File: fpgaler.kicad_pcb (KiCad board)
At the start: 2 copper layers, 0 parts

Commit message: start to assign footprint
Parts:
- added C1: 100nF, Capacitor_SMD:C_0603_1608Metric, F.Cu at (130.2, 113.1)
- added C10: 4.7uF, Capacitor_SMD:C_0805_2012Metric, F.Cu at (169.7, 49.9)
- added C11: 4.7uF, Capacitor_SMD:C_0805_2012Metric, F.Cu at (169.7, 52.9)
- added C12: 10uF, Capacitor_SMD:C_1206_3216Metric, F.Cu at (164.7, 50.1)
- added C13: 10uF, Capacitor_SMD:C_1206_3216Metric, F.Cu at (164.7, 53.5)
- added C14: 4.7uF, Capacitor_SMD:C_0805_2012Metric, F.Cu at (169.7, 56.0)
- added C15: 10pF, Capacitor_SMD:C_0603_1608Metric, F.Cu at (151.8, 52.2)
- added C16: 10pF, Capacitor_SMD:C_0603_1608Metric, F.Cu at (151.8, 54.7)
- added C17: 4.7uF, Capacitor_SMD:C_0805_2012Metric, F.Cu at (169.7, 59.0)
- added C18: 10uF, Capacitor_SMD:C_1206_3216Metric, F.Cu at (164.7, 56.8)
- added C19: 10uF, Capacitor_SMD:C_1206_3216Metric, F.Cu at (164.7, 60.1)
- added C2: 4.7uF, Capacitor_SMD:C_0805_2012Metric, F.Cu at (113.3, 131.0)
- added C20: 10uF, Capacitor_SMD:C_1206_3216Metric, F.Cu at (164.7, 63.5)
- added C21: 10uF, Capacitor_SMD:C_1206_3216Metric, F.Cu at (164.7, 66.8)
- added C22: 100nF, Capacitor_SMD:C_0603_1608Metric, F.Cu at (148.3, 90.7)
- added C23: 18pF, Capacitor_SMD:C_0603_1608Metric, F.Cu at (148.3, 93.2)
- added C24: 18pF, Capacitor_SMD:C_0603_1608Metric, F.Cu at (148.3, 95.8)
- added C25: 10uF, Capacitor_SMD:C_1206_3216Metric, F.Cu at (165.1, 105.6)
- added C26: 100nF, Capacitor_SMD:C_0603_1608Metric, F.Cu at (148.3, 98.3)
- added C27: 100nF, Capacitor_SMD:C_0603_1608Metric, F.Cu at (148.3, 100.8)
- added C28: 100nF, Capacitor_SMD:C_0603_1608Metric, F.Cu at (148.3, 103.3)
- added C29: 100nF, Capacitor_SMD:C_0603_1608Metric, F.Cu at (148.3, 105.8)
- added C3: 100nF, Capacitor_SMD:C_0603_1608Metric, F.Cu at (130.2, 115.6)
- added C30: 100nF, Capacitor_SMD:C_0603_1608Metric, F.Cu at (148.3, 108.3)
- added C31: 100nF, Capacitor_SMD:C_0603_1608Metric, F.Cu at (148.3, 110.8)
- added C32: 100nF, Capacitor_SMD:C_0603_1608Metric, F.Cu at (152.3, 90.7)
- added C33: 10uF, Capacitor_SMD:C_1206_3216Metric, F.Cu at (165.1, 109.0)
- added C34: 100nF, Capacitor_SMD:C_0603_1608Metric, F.Cu at (152.3, 93.2)
- added C35: 100nF, Capacitor_SMD:C_0603_1608Metric, F.Cu at (152.3, 95.8)
- added C36: 4.7uF, Capacitor_SMD:C_0805_2012Metric, F.Cu at (170.2, 105.4)
- added C37: 4.7uF, Capacitor_SMD:C_0805_2012Metric, F.Cu at (170.2, 108.4)
- added C38: 100nF, Capacitor_SMD:C_0603_1608Metric, F.Cu at (129.8, 49.7)
- added C39: 100nF, Capacitor_SMD:C_0603_1608Metric, F.Cu at (129.8, 52.2)
- added C4: 100nF, Capacitor_SMD:C_0603_1608Metric, F.Cu at (130.2, 118.1)
- added C40: 10nF, Capacitor_SMD:C_0603_1608Metric, F.Cu at (148.3, 117.8)
- added C41: 10nF, Capacitor_SMD:C_0603_1608Metric, F.Cu at (148.3, 120.3)
- added C42: 10nF, Capacitor_SMD:C_0603_1608Metric, F.Cu at (148.3, 122.8)
- added C43: 100nF, Capacitor_SMD:C_0603_1608Metric, F.Cu at (148.3, 125.3)
- added C44: 100nF, Capacitor_SMD:C_0603_1608Metric, F.Cu at (148.3, 127.8)
- added C45: 100nF, Capacitor_SMD:C_0603_1608Metric, F.Cu at (148.3, 130.3)
- added C46: 10nF, Capacitor_SMD:C_0603_1608Metric, F.Cu at (148.3, 132.8)
- added C47: 10nF, Capacitor_SMD:C_0603_1608Metric, F.Cu at (152.3, 117.8)
- added C48: 10nF, Capacitor_SMD:C_0603_1608Metric, F.Cu at (152.3, 120.3)
- added C49: 100nF, Capacitor_SMD:C_0603_1608Metric, F.Cu at (152.3, 122.8)
- added C5: 100nF, Capacitor_SMD:C_0603_1608Metric, F.Cu at (130.2, 120.6)
- added C50: 100nF, Capacitor_SMD:C_0603_1608Metric, F.Cu at (152.3, 125.3)
- added C51: 100nF, Capacitor_SMD:C_0603_1608Metric, F.Cu at (152.3, 127.8)
- added C52: 10nF, Capacitor_SMD:C_0603_1608Metric, F.Cu at (152.3, 130.3)
- added C53: 10nF, Capacitor_SMD:C_0603_1608Metric, F.Cu at (152.3, 132.8)
- added C54: 100nF, Capacitor_SMD:C_0603_1608Metric, F.Cu at (156.3, 117.8)
- added C55: 100nF, Capacitor_SMD:C_0603_1608Metric, F.Cu at (156.3, 120.3)
- added C6: 100nF, Capacitor_SMD:C_0603_1608Metric, F.Cu at (130.2, 123.1)
- added C7: 100nF, Capacitor_SMD:C_0603_1608Metric, F.Cu at (130.2, 125.7)
- added C8: 100nF, Capacitor_SMD:C_0603_1608Metric, F.Cu at (130.2, 128.2)
- added C9: 100nF, Capacitor_SMD:C_0603_1608Metric, F.Cu at (151.8, 49.7)
- added D1: L0, Diode_SMD:D_0603_1608Metric, F.Cu at (134.8, 90.8)
- added D10: LED, Diode_SMD:D_0603_1608Metric, F.Cu at (164.3, 124.9)
- added D11: LED, Diode_SMD:D_0603_1608Metric, F.Cu at (164.3, 127.5)
- added D2: L1, Diode_SMD:D_0603_1608Metric, F.Cu at (134.8, 93.4)
- added D3: L2, Diode_SMD:D_0603_1608Metric, F.Cu at (134.8, 96.0)
- added D4: L3, Diode_SMD:D_0603_1608Metric, F.Cu at (134.8, 98.5)
- added D5: L4, Diode_SMD:D_0603_1608Metric, F.Cu at (134.8, 101.1)
- added D6: L5, Diode_SMD:D_0603_1608Metric, F.Cu at (134.8, 103.7)
- added D7: L6, Diode_SMD:D_0603_1608Metric, F.Cu at (134.8, 106.3)
- added D8: L7, Diode_SMD:D_0603_1608Metric, F.Cu at (134.8, 108.9)
- added FB2: BLM18HE152SN1D, Inductor_SMD:L_0603_1608Metric, F.Cu at (152.3, 98.3)
- added FB3: BLM18HE152SN1D, Inductor_SMD:L_0603_1608Metric, F.Cu at (152.3, 100.8)
- added J1: USB_C_Receptacle_USB2.0, Connector_USB:USB_C_Receptacle_HRO_TYPE-C-31-M-12, F.Cu at (105.2, 128.2)
- added J3: Conn_01x08_MountingPin, Connector_PinHeader_2.54mm:PinHeader_1x08_P2.54mm_Vertical, F.Cu at (130.5, 91.8)
- added J4: FTDI_RST, Connector_PinHeader_2.54mm:PinHeader_1x02_P2.54mm_Vertical, F.Cu at (113.3, 124.7)
- added L1: 2.2uH, Inductor_SMD:L_0805_2012Metric, F.Cu at (157.7, 64.9)
- added L2: 2.2uH, Inductor_SMD:L_0805_2012Metric, F.Cu at (157.7, 67.6)
- added Q1: 2N2222/SOT23, Package_TO_SOT_SMD:SOT-23-3, F.Cu at (164.9, 131.0)
- added R1: 10k, Resistor_SMD:R_0603_1608Metric, F.Cu at (130.2, 130.7)
- added R10: 22R, Resistor_SMD:R_0603_1608Metric, F.Cu at (138.2, 113.1)
- added R11: 10k, Resistor_SMD:R_0603_1608Metric, F.Cu at (138.2, 115.6)
- added R12: 1.2k, Resistor_SMD:R_0603_1608Metric, F.Cu at (138.2, 118.1)
- added R13: 1.2k, Resistor_SMD:R_0603_1608Metric, F.Cu at (138.2, 120.6)
- added R14: 1.2k, Resistor_SMD:R_0603_1608Metric, F.Cu at (138.2, 123.1)
- added R15: 10k, Resistor_SMD:R_0603_1608Metric, F.Cu at (138.2, 125.7)
- added R16: 1.2k, Resistor_SMD:R_0603_1608Metric, F.Cu at (138.2, 128.2)
- added R17: 10k, Resistor_SMD:R_0603_1608Metric, F.Cu at (138.2, 130.7)
- added R18: 1.2k, Resistor_SMD:R_0603_1608Metric, F.Cu at (142.2, 113.1)
- added R19: 10k, Resistor_SMD:R_0603_1608Metric, F.Cu at (142.2, 115.6)
- added R2: 10k, Resistor_SMD:R_0603_1608Metric, F.Cu at (134.2, 113.1)
- added R20: 1.2k, Resistor_SMD:R_0603_1608Metric, F.Cu at (142.2, 118.1)
- added R21: 1.2k, Resistor_SMD:R_0603_1608Metric, F.Cu at (142.2, 120.6)
- added R22: 10k, Resistor_SMD:R_0603_1608Metric, F.Cu at (142.2, 123.1)
- added R23: 1.2k, Resistor_SMD:R_0603_1608Metric, F.Cu at (142.2, 125.7)
- added R24: 10k, Resistor_SMD:R_0603_1608Metric, F.Cu at (142.2, 128.2)
- added R25: 10k, Resistor_SMD:R_0603_1608Metric, F.Cu at (151.8, 57.2)
- added R26: 4.7k, Resistor_SMD:R_0603_1608Metric, F.Cu at (151.8, 59.7)
- added R27: 3.57k, Resistor_SMD:R_0603_1608Metric, F.Cu at (151.8, 62.2)
- added R28: 56.2k, Resistor_SMD:R_0603_1608Metric, F.Cu at (155.8, 49.7)
- added R29: 3.09k, Resistor_SMD:R_0603_1608Metric, F.Cu at (155.8, 52.2)
- added R3: 10k, Resistor_SMD:R_0603_1608Metric, F.Cu at (134.2, 115.6)
- added R30: 4.32k, Resistor_SMD:R_0603_1608Metric, F.Cu at (155.8, 54.7)
- added R31: 10k, Resistor_SMD:R_0603_1608Metric, F.Cu at (155.8, 57.2)
- added R32: 10k, Resistor_SMD:R_0603_1608Metric, F.Cu at (155.8, 59.7)
- added R33: DNP, Resistor_SMD:R_0603_1608Metric, F.Cu at (155.8, 62.2)
- added R34: 100k, Resistor_SMD:R_0603_1608Metric, F.Cu at (159.8, 49.7)
- added R35: 120k, Resistor_SMD:R_0603_1608Metric, F.Cu at (159.8, 52.2)
- added R36: 360k, Resistor_SMD:R_0603_1608Metric, F.Cu at (159.8, 54.7)
- added R37: 82k, Resistor_SMD:R_0603_1608Metric, F.Cu at (159.8, 57.2)
- added R38: 10k, Resistor_SMD:R_0603_1608Metric, F.Cu at (152.3, 103.3)
- added R39: 10k, Resistor_SMD:R_0603_1608Metric, F.Cu at (152.3, 105.8)
- added R4: 10k, Resistor_SMD:R_0603_1608Metric, F.Cu at (134.2, 118.1)
- added R40: 10k, Resistor_SMD:R_0603_1608Metric, F.Cu at (152.3, 108.3)
- added R41: 12k, Resistor_SMD:R_0603_1608Metric, F.Cu at (152.3, 110.8)
- added R42: 2.2k, Resistor_SMD:R_0603_1608Metric, F.Cu at (156.3, 90.7)
- added R43: 0R, Resistor_SMD:R_0603_1608Metric, F.Cu at (156.3, 93.2)
- added R44: 12k, Resistor_SMD:R_0603_1608Metric, F.Cu at (156.3, 95.8)
- added R45: 2.2k, Resistor_SMD:R_0603_1608Metric, F.Cu at (156.3, 98.3)
- added R46: 22R, Resistor_SMD:R_0603_1608Metric, F.Cu at (156.3, 100.8)
- added R47: 22R, Resistor_SMD:R_0603_1608Metric, F.Cu at (156.3, 103.3)
- added R48: 22R, Resistor_SMD:R_0603_1608Metric, F.Cu at (156.3, 105.8)
- added R49: 22R, Resistor_SMD:R_0603_1608Metric, F.Cu at (156.3, 108.3)
- added R5: 5.1k, Resistor_SMD:R_0603_1608Metric, F.Cu at (134.2, 120.6)
- added R50: 22R, Resistor_SMD:R_0603_1608Metric, F.Cu at (156.3, 110.8)
- added R51: 22R, Resistor_SMD:R_0603_1608Metric, F.Cu at (160.3, 90.7)
- added R52: 2.2k, Resistor_SMD:R_0603_1608Metric, F.Cu at (160.3, 93.2)
- added R53: 22R, Resistor_SMD:R_0603_1608Metric, F.Cu at (160.3, 95.8)
- added R54: 22R, Resistor_SMD:R_0603_1608Metric, F.Cu at (160.3, 98.3)
- added R55: 22R, Resistor_SMD:R_0603_1608Metric, F.Cu at (160.3, 100.8)
- added R56: 2.2k, Resistor_SMD:R_0603_1608Metric, F.Cu at (160.3, 103.3)
- added R57: 4.7k, Resistor_SMD:R_0603_1608Metric, F.Cu at (160.3, 105.8)
- added R58: 4.7k, Resistor_SMD:R_0603_1608Metric, F.Cu at (160.3, 108.3)
- added R59: 4.7k, Resistor_SMD:R_0603_1608Metric, F.Cu at (160.3, 110.8)
- added R6: 5.1k, Resistor_SMD:R_0603_1608Metric, F.Cu at (134.2, 123.1)
- added R60: 4.7k, Resistor_SMD:R_0603_1608Metric, F.Cu at (129.8, 54.7)
- added R61: 22R, Resistor_SMD:R_0603_1608Metric, F.Cu at (129.8, 57.2)
- added R62: 22R, Resistor_SMD:R_0603_1608Metric, F.Cu at (129.8, 59.7)
- added R63: 22R, Resistor_SMD:R_0603_1608Metric, F.Cu at (129.8, 62.2)
- added R64: 22R, Resistor_SMD:R_0603_1608Metric, F.Cu at (133.8, 49.7)
- added R65: 4.7k, Resistor_SMD:R_0603_1608Metric, F.Cu at (133.8, 52.2)
- added R66: 4.7k, Resistor_SMD:R_0603_1608Metric, F.Cu at (133.8, 54.7)
- added R67: 22R, Resistor_SMD:R_0603_1608Metric, F.Cu at (133.8, 57.2)
- added R68: 22R, Resistor_SMD:R_0603_1608Metric, F.Cu at (133.8, 59.7)
- added R69: 22R, Resistor_SMD:R_0603_1608Metric, F.Cu at (133.8, 62.2)
- added R7: 10k, Resistor_SMD:R_0603_1608Metric, F.Cu at (134.2, 125.7)
- added R70: 22R, Resistor_SMD:R_0603_1608Metric, F.Cu at (137.8, 49.7)
- added R71: 22R, Resistor_SMD:R_0603_1608Metric, F.Cu at (137.8, 52.2)
- added R72: 22R, Resistor_SMD:R_0603_1608Metric, F.Cu at (137.8, 54.7)
- added R73: 22R, Resistor_SMD:R_0603_1608Metric, F.Cu at (137.8, 57.2)
- added R74: 22R, Resistor_SMD:R_0603_1608Metric, F.Cu at (137.8, 59.7)
- added R75: 22R, Resistor_SMD:R_0603_1608Metric, F.Cu at (137.8, 62.2)
- added R76: 22R, Resistor_SMD:R_0603_1608Metric, F.Cu at (141.8, 49.7)
- added R77: 22R, Resistor_SMD:R_0603_1608Metric, F.Cu at (141.8, 52.2)
- added R78: 22R, Resistor_SMD:R_0603_1608Metric, F.Cu at (141.8, 54.7)
- added R79: 22R, Resistor_SMD:R_0603_1608Metric, F.Cu at (141.8, 57.2)
- added R8: 10k, Resistor_SMD:R_0603_1608Metric, F.Cu at (134.2, 128.2)
- added R80: 22R, Resistor_SMD:R_0603_1608Metric, F.Cu at (141.8, 59.7)
- added R81: 22R, Resistor_SMD:R_0603_1608Metric, F.Cu at (141.8, 62.2)
- added R82: 22R, Resistor_SMD:R_0603_1608Metric, F.Cu at (145.8, 49.7)
- added R83: 22R, Resistor_SMD:R_0603_1608Metric, F.Cu at (145.8, 52.2)
- added R84: 22R, Resistor_SMD:R_0603_1608Metric, F.Cu at (145.8, 54.7)
- added R85: 4.7k, Resistor_SMD:R_0603_1608Metric, F.Cu at (145.8, 57.2)
- added R86: 4.7k, Resistor_SMD:R_0603_1608Metric, F.Cu at (145.8, 59.7)
- added R87: 4.7k, Resistor_SMD:R_0603_1608Metric, F.Cu at (145.8, 62.2)
- added R88: 1.5k, Resistor_SMD:R_0603_1608Metric, F.Cu at (156.3, 122.8)
- added R89: 2.2k, Resistor_SMD:R_0603_1608Metric, F.Cu at (156.3, 125.3)
- added R9: 22R, Resistor_SMD:R_0603_1608Metric, F.Cu at (134.2, 130.7)
- added R90: 4.7k, Resistor_SMD:R_0603_1608Metric, F.Cu at (156.3, 127.8)
- added R91: 4.7k, Resistor_SMD:R_0603_1608Metric, F.Cu at (156.3, 130.3)
- added R92: 4.7k, Resistor_SMD:R_0603_1608Metric, F.Cu at (156.3, 132.8)
- added R93: 2.2k, Resistor_SMD:R_0603_1608Metric, F.Cu at (160.3, 117.8)
- added R94: 2.2k, Resistor_SMD:R_0603_1608Metric, F.Cu at (160.3, 120.3)
- added R95: 10k, Resistor_SMD:R_0603_1608Metric, F.Cu at (160.3, 122.8)
- added R96: 10k, Resistor_SMD:R_0603_1608Metric, F.Cu at (160.3, 125.3)
- added SW1: RotaryEncoder_Switch, Rotary_Encoder:RotaryEncoder_Alps_EC11E-Switch_Vertical_H20mm_CircularMountingHoles, F.Cu at (101.4, 95.2)
- added SW2: RotaryEncoder_Switch, Rotary_Encoder:RotaryEncoder_Alps_EC11E-Switch_Vertical_H20mm_CircularMountingHoles, F.Cu at (101.4, 111.7)
- added SW3: K1, Button_Switch_THT:SW_PUSH_1P1T_6x3.5mm_H4.3_APEM_MJTP1243, F.Cu at (119.8, 92.0)
- added SW4: K2, Button_Switch_THT:SW_PUSH_1P1T_6x3.5mm_H4.3_APEM_MJTP1243, F.Cu at (119.8, 97.0)
- added SW5: PROGRAMN, Button_Switch_THT:SW_PUSH_1P1T_6x3.5mm_H4.3_APEM_MJTP1243, F.Cu at (119.8, 102.1)
- added SW6: K3, Button_Switch_THT:SW_PUSH_1P1T_6x3.5mm_H4.3_APEM_MJTP1243, F.Cu at (119.8, 107.2)
- added SW7: FPGA GSRN, Button_Switch_THT:SW_PUSH_1P1T_6x3.5mm_H4.3_APEM_MJTP1243, F.Cu at (119.8, 112.2)
- added SW8: K4, Button_Switch_THT:SW_PUSH_1P1T_6x3.5mm_H4.3_APEM_MJTP1243, F.Cu at (119.8, 117.2)
- added TP1: TestPoint, TestPoint:TestPoint_Pad_D1.0mm, F.Cu at (174.7, 111.5)
- added TP10: TestPoint, TestPoint:TestPoint_THTPad_D1.5mm_Drill0.7mm, F.Cu at (101.1, 78.6)
- added TP11: TestPoint, TestPoint:TestPoint_THTPad_D1.5mm_Drill0.7mm, F.Cu at (101.1, 82.2)
- added TP12: TestPoint, TestPoint:TestPoint_THTPad_D1.5mm_Drill0.7mm, F.Cu at (101.1, 85.7)
- added TP13: TestPoint, TestPoint:TestPoint_THTPad_D1.5mm_Drill0.7mm, F.Cu at (104.7, 50.2)
- added TP14: TestPoint, TestPoint:TestPoint_THTPad_D1.5mm_Drill0.7mm, F.Cu at (104.7, 53.8)
- added TP15: TestPoint, TestPoint:TestPoint_THTPad_D1.5mm_Drill0.7mm, F.Cu at (104.7, 57.3)
- added TP16: TestPoint, TestPoint:TestPoint_THTPad_D1.5mm_Drill0.7mm, F.Cu at (104.7, 60.9)
- added TP17: TestPoint, TestPoint:TestPoint_THTPad_D1.5mm_Drill0.7mm, F.Cu at (104.7, 64.4)
- added TP18: TestPoint, TestPoint:TestPoint_THTPad_D1.5mm_Drill0.7mm, F.Cu at (104.7, 68.0)
- added TP19: TestPoint, TestPoint:TestPoint_THTPad_D1.5mm_Drill0.7mm, F.Cu at (104.7, 71.5)
- added TP2: TestPoint, TestPoint:TestPoint_THTPad_D1.5mm_Drill0.7mm, F.Cu at (101.1, 50.2)
- added TP20: TestPoint, TestPoint:TestPoint_THTPad_D1.5mm_Drill0.7mm, F.Cu at (104.7, 75.0)
- added TP21: TestPoint, TestPoint:TestPoint_THTPad_D1.5mm_Drill0.7mm, F.Cu at (104.7, 78.6)
- added TP22: TestPoint, TestPoint:TestPoint_THTPad_D1.5mm_Drill0.7mm, F.Cu at (104.7, 82.2)
- added TP23: TestPoint, TestPoint:TestPoint_THTPad_D1.5mm_Drill0.7mm, F.Cu at (104.7, 85.7)
- added TP24: TestPoint, TestPoint:TestPoint_THTPad_D1.5mm_Drill0.7mm, F.Cu at (108.2, 50.2)
- added TP25: TestPoint, TestPoint:TestPoint_THTPad_D1.5mm_Drill0.7mm, F.Cu at (108.2, 53.8)
- added TP26: TestPoint, TestPoint:TestPoint_THTPad_D1.5mm_Drill0.7mm, F.Cu at (108.2, 57.3)
- added TP27: TestPoint, TestPoint:TestPoint_THTPad_D1.5mm_Drill0.7mm, F.Cu at (108.2, 60.9)
- added TP28: TestPoint, TestPoint:TestPoint_THTPad_D1.5mm_Drill0.7mm, F.Cu at (108.2, 64.4)
- added TP29: TestPoint, TestPoint:TestPoint_THTPad_D1.5mm_Drill0.7mm, F.Cu at (108.2, 68.0)
- added TP3: TestPoint, TestPoint:TestPoint_THTPad_D1.5mm_Drill0.7mm, F.Cu at (101.1, 53.8)
- added TP30: TestPoint, TestPoint:TestPoint_THTPad_D1.5mm_Drill0.7mm, F.Cu at (108.2, 71.5)
- added TP31: TestPoint, TestPoint:TestPoint_THTPad_D1.5mm_Drill0.7mm, F.Cu at (108.2, 75.0)
- added TP32: TestPoint, TestPoint:TestPoint_THTPad_D1.5mm_Drill0.7mm, F.Cu at (108.2, 78.6)
- added TP33: TestPoint, TestPoint:TestPoint_THTPad_D1.5mm_Drill0.7mm, F.Cu at (108.2, 82.2)
- added TP34: TestPoint, TestPoint:TestPoint_THTPad_D1.5mm_Drill0.7mm, F.Cu at (108.2, 85.7)
- added TP35: TestPoint, TestPoint:TestPoint_THTPad_D1.5mm_Drill0.7mm, F.Cu at (111.8, 50.2)
- added TP36: TestPoint, TestPoint:TestPoint_THTPad_D1.5mm_Drill0.7mm, F.Cu at (111.8, 53.8)
- added TP37: TestPoint, TestPoint:TestPoint_THTPad_D1.5mm_Drill0.7mm, F.Cu at (111.8, 57.3)
- added TP38: TestPoint, TestPoint:TestPoint_THTPad_D1.5mm_Drill0.7mm, F.Cu at (111.8, 60.9)
- added TP39: TestPoint, TestPoint:TestPoint_THTPad_D1.5mm_Drill0.7mm, F.Cu at (111.8, 64.4)
- added TP4: TestPoint, TestPoint:TestPoint_THTPad_D1.5mm_Drill0.7mm, F.Cu at (101.1, 57.3)
- added TP40: TestPoint, TestPoint:TestPoint_THTPad_D1.5mm_Drill0.7mm, F.Cu at (111.8, 68.0)
- added TP41: TestPoint, TestPoint:TestPoint_THTPad_D1.5mm_Drill0.7mm, F.Cu at (111.8, 71.5)
- added TP42: TestPoint, TestPoint:TestPoint_THTPad_D1.5mm_Drill0.7mm, F.Cu at (111.8, 75.0)
- added TP43: TestPoint, TestPoint:TestPoint_THTPad_D1.5mm_Drill0.7mm, F.Cu at (111.8, 78.6)
- added TP44: TestPoint, TestPoint:TestPoint_THTPad_D1.5mm_Drill0.7mm, F.Cu at (111.8, 82.2)
- added TP45: TestPoint, TestPoint:TestPoint_THTPad_D1.5mm_Drill0.7mm, F.Cu at (111.8, 85.7)
- added TP46: TestPoint, TestPoint:TestPoint_THTPad_D1.5mm_Drill0.7mm, F.Cu at (115.3, 50.2)
- added TP47: TestPoint, TestPoint:TestPoint_THTPad_D1.5mm_Drill0.7mm, F.Cu at (115.3, 53.8)
- added TP48: TestPoint, TestPoint:TestPoint_THTPad_D1.5mm_Drill0.7mm, F.Cu at (115.3, 57.3)
- added TP49: TestPoint, TestPoint:TestPoint_THTPad_D1.5mm_Drill0.7mm, F.Cu at (115.3, 60.9)
- added TP5: TestPoint, TestPoint:TestPoint_THTPad_D1.5mm_Drill0.7mm, F.Cu at (101.1, 60.9)
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
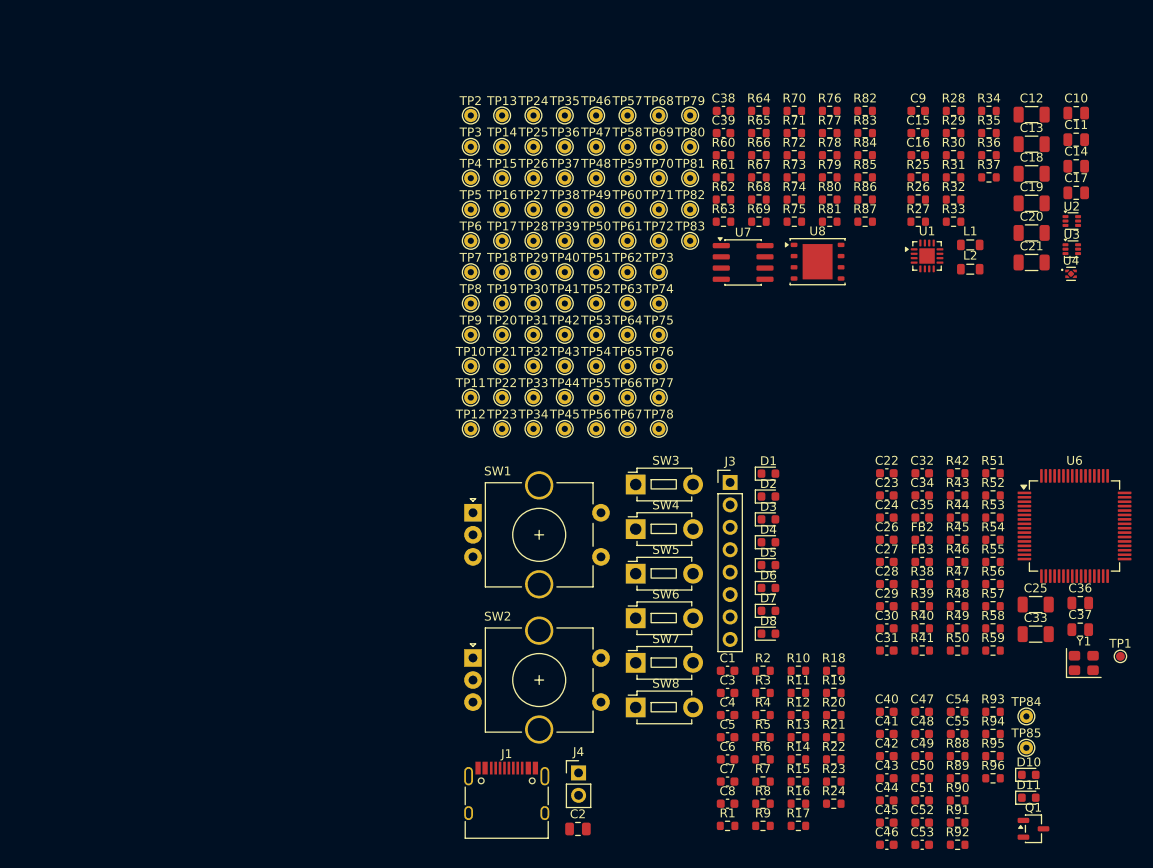
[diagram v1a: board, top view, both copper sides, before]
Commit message: Assign jlcpcb pn. Fix footprint assign, uniform resistor value for battery charger
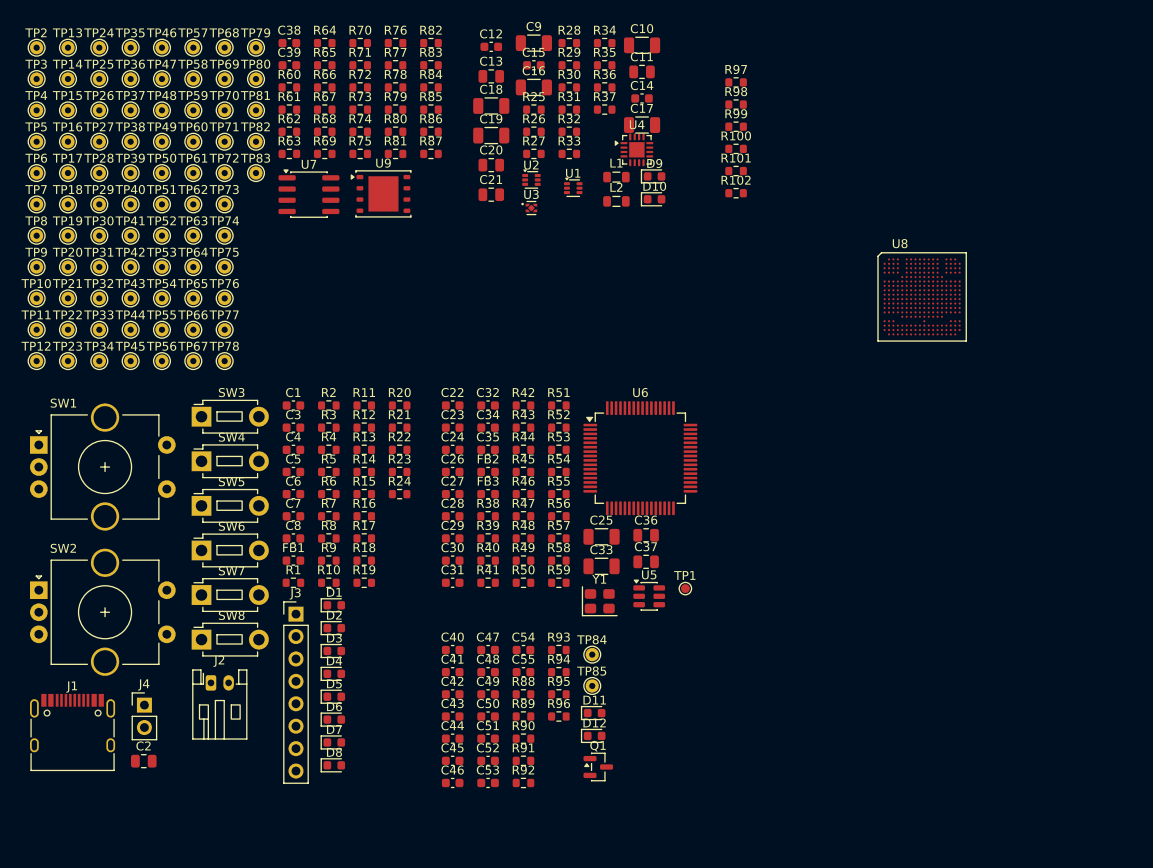
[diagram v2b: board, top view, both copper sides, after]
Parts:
- added D12: LED, Diode_SMD:D_0603_1608Metric, F.Cu at (115.2, 120.5)
- added D9: PRESENT, Diode_SMD:D_0603_1608Metric, F.Cu at (121.9, 57.1)
- added FB1: CBG160808U150T, Inductor_SMD:L_0603_1608Metric, F.Cu at (81.0, 100.6)
- added J2: BATT, Connector_JST:JST_PH_S2B-PH-K_1x02_P2.00mm_Horizontal, F.Cu at (71.7, 114.5)
- added R100: 2.2k, Resistor_SMD:R_0603_1608Metric, F.Cu at (131.2, 54.0)
- added R101: 10k, Resistor_SMD:R_0603_1608Metric, F.Cu at (131.2, 56.5)
- added R102: 10k, Resistor_SMD:R_0603_1608Metric, F.Cu at (131.2, 59.0)
- added R97: 4.7k, Resistor_SMD:R_0603_1608Metric, F.Cu at (131.2, 46.5)
- added R98: 4.7k, Resistor_SMD:R_0603_1608Metric, F.Cu at (131.2, 49.0)
- added R99: 2.2k, Resistor_SMD:R_0603_1608Metric, F.Cu at (131.2, 51.5)
- added U5: 93LC56BT-I/OT, Package_TO_SOT_SMD:SOT-23-6, F.Cu at (121.3, 104.7)
- added U9: W25Q128JVP, Package_SON:WSON-8-1EP_6x5mm_P1.27mm_EP3.4x4mm, F.Cu at (91.2, 59.1)
- C10, C17: value 4.7uF -> 10uF; footprint Capacitor_SMD:C_0805_2012Metric -> Capacitor_SMD:C_1206_3216Metric
- C12: value 10uF -> 100nF; footprint Capacitor_SMD:C_1206_3216Metric -> Capacitor_SMD:C_0603_1608Metric
- C13, C20, C21: value 10uF -> 4.7uF; footprint Capacitor_SMD:C_1206_3216Metric -> Capacitor_SMD:C_0805_2012Metric
- C14: value 4.7uF -> 10pF; footprint Capacitor_SMD:C_0805_2012Metric -> Capacitor_SMD:C_0603_1608Metric
- C16: value 10pF -> 10uF; footprint Capacitor_SMD:C_0603_1608Metric -> Capacitor_SMD:C_1206_3216Metric
- C9: value 100nF -> 10uF; footprint Capacitor_SMD:C_0603_1608Metric -> Capacitor_SMD:C_1206_3216Metric
- D10: value LED -> CHARGER
- FB2, FB3: value BLM18HE152SN1D -> CBG160808U150T
- J3: value Conn_01x08_MountingPin -> JTAG
- Q1: value 2N2222/SOT23 -> BC817; footprint Package_TO_SOT_SMD:SOT-23-3 -> Package_TO_SOT_SMD:SOT-23
- R27: value 3.57k -> 10k
- R28: value 56.2k -> DNP
- R29: value 3.09k -> 120k
- R30: value 4.32k -> 120k
- R31: value 10k -> 360k
- R32: value 10k -> 82k
- R34: value 100k -> DNP
- R35: value 120k -> 3.9k
- R36: value 360k -> 39k
- R37: value 82k -> 68k
- R38: value 10k -> 330k
- R39: value 10k -> 3.3k
- R40: value 10k -> 47k
- R41: value 12k -> 4.7k
- R42: value 2.2k -> 56k
- R43: value 0R -> 10k
- R44: value 12k -> 10k
- R45: value 2.2k -> 10k
- R46: value 22R -> 10k
- R47, R50: value 22R -> 12k
- R48, R51, R62: value 22R -> 2.2k
- R49: value 22R -> 0R
- R52, R56, R89: value 2.2k -> 22R
- R57, R59, R60, R85, R86, R87, R90: value 4.7k -> 22R
- R58: value 4.7k -> 2.2k
- R63, R64, R71, R72: value 22R -> 4.7k
- R88: value 1.5k -> 22R
- R93: value 2.2k -> 4.7k
- R94: value 2.2k -> 1.5k
- R95: value 10k -> 2.2k
- R96: value 10k -> 4.7k
- U1: value BQ24232 -> TLV62569DRL; footprint Package_DFN_QFN:QFN-16-1EP_3x3mm_P0.5mm_EP1.75x1.75mm -> Package_TO_SOT_SMD:SOT-563
- U3: value TLV62569DRL -> NCP115-2.5; footprint Package_TO_SOT_SMD:SOT-563 -> Package_SON:Texas_X2SON-4_1x1mm_P0.65mm
- U4: value NCP115-2.5 -> BQ24232; footprint Package_SON:Texas_X2SON-4_1x1mm_P0.65mm -> Package_DFN_QFN:QFN-16-1EP_3x3mm_P0.5mm_EP1.75x1.75mm
- U8: value W25Q128JVP -> LFE5U-25F-8MG285C; footprint Package_SON:WSON-8-1EP_6x5mm_P1.27mm_EP3.4x4mm -> kicad:BGA-285
- moved D10 77.8 mm to (121.9, 59.7)
- moved C12 61.7 mm to (103.4, 42.4)
- moved C13 61.7 mm to (103.4, 45.8)
- moved C18 61.7 mm to (103.4, 49.1)
- moved C19 61.7 mm to (103.4, 52.5)
- moved C20 61.7 mm to (103.4, 55.8)
- moved C21 61.7 mm to (103.4, 59.2)
- moved U2 61.4 mm to (108.0, 57.5)
- moved U3 61.4 mm to (108.0, 60.7)
- moved R20 60.4 mm to (93.1, 83.0)
- moved R21 60.4 mm to (93.1, 85.6)
- moved R22 60.4 mm to (93.1, 88.1)
- moved R23 60.4 mm to (93.1, 90.6)
- moved R24 60.4 mm to (93.1, 93.1)
- moved R11 59.0 mm to (89.1, 83.0)
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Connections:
- C10 pad 1: VSYS -> GND
- C10 pad 2: GND -> VSYS
- C11 pad 1: VBATT -> +3.3V
- C12 pad 1: GND -> +5V
- C12 pad 2: VSYS -> GND
- C13 pad 1: GND -> +2.5V
- C13 pad 2: VSYS -> GND
- C14 pad 1: +3.3V -> Net-(U1-FB)
- C14 pad 2: GND -> +1.1V
- C15 pad 2: +1.1V -> +3.3V
- C16 pad 1: Net-(U3-FB) -> GND
- C16 pad 2: +3.3V -> +1.1V
- C17 pad 1: +2.5V -> GND
- C17 pad 2: GND -> +3.3V
- C20 pad 1: GND -> VSYS
- C20 pad 2: +1.1V -> GND
- C21 pad 1: GND -> VBATT
- C21 pad 2: +3.3V -> GND
- C9 pad 1: +5V -> GND
- C9 pad 2: GND -> VSYS
- D10 pad 2: Net-(D10-A) -> VSYS
- D11 pad 1: /FPGA PWR/INITN -> Net-(D11-K)
- L1 pad 1: Net-(U2-SW) -> Net-(U1-SW)
- L2 pad 1: Net-(U3-SW) -> Net-(U2-SW)
- Q1 pad 2: Net-(D10-K) -> GND
- Q1 pad 3: GND -> Net-(D11-K)
- R25 pad 1: Net-(U1-~{PGOOD}) -> Net-(U4-~{PGOOD})
- R26 pad 1: Net-(U1-~{CHG}) -> Net-(U4-~{CHG})
- R26 pad 2: Net-(D9-RK) -> Net-(D10-K)
- R27 pad 1: GND -> EN
- R27 pad 2: Net-(U1-TD) -> VSYS
- R28 pad 1: GND -> EN
- R28 pad 2: Net-(U1-TMR) -> VSYS
- R29 pad 1: GND -> +1.1V
- R29 pad 2: Net-(U1-ILIM) -> Net-(U1-FB)
- R30 pad 1: GND -> Net-(U1-FB)
- R30 pad 2: Net-(U1-ISET) -> GND
- R31 pad 1: GND -> Net-(U2-FB)
- R31 pad 2: Net-(U1-TS) -> +3.3V
- R32 pad 1: EN -> Net-(U2-FB)
- R32 pad 2: VSYS -> GND
- R33 pad 1: EN -> Net-(R33-Pad1)
- R33 pad 2: VSYS -> +3.3V
- R34 pad 1: Net-(U2-FB) -> Net-(R33-Pad1)
- R34 pad 2: +1.1V -> GND
- R35 pad 1: Net-(U2-FB) -> GND
- R35 pad 2: GND -> Net-(U4-TD)
- R36 pad 1: Net-(U3-FB) -> GND
- R36 pad 2: +3.3V -> Net-(U4-TD)
- R37 pad 1: Net-(U3-FB) -> GND
- R37 pad 2: GND -> Net-(U4-TMR)
- R38 pad 1: +3.3V -> GND
- R38 pad 2: /FTDI/EE_CS -> Net-(U4-TMR)
- R39 pad 1: /FTDI/EE_CLK -> GND
- R39 pad 2: +3.3V -> Net-(U4-ILIM)
- R40 pad 1: Net-(U5-DO) -> GND
- R40 pad 2: +3.3V -> Net-(U4-ILIM)
- R41 pad 1: /FTDI/EE_DAT -> GND
- R41 pad 2: Net-(U5-DO) -> Net-(U4-ISET)
- R42 pad 1: +3.3V -> GND
- R42 pad 2: /FTDI/FT_RESET -> Net-(U4-ISET)
- R43 pad 1: /FPGA/REF_CLK -> GND
- R43 pad 2: Net-(U6-OSCO) -> Net-(U4-TS)
- R44 pad 1: Net-(U6-REF) -> +3.3V
- R44 pad 2: GND -> /FTDI/EE_CS
- R45 pad 1: Net-(U6-BDBUS1) -> /FTDI/EE_CLK
- R46 pad 1: Net-(U6-ADBUS0) -> Net-(U5-DO)
- R46 pad 2: /FT_TCK -> +3.3V
- R47 pad 1: Net-(U6-ADBUS1) -> /FTDI/EE_DAT
- R47 pad 2: /FT_TDI -> Net-(U5-DO)
- R48 pad 1: Net-(U6-ADBUS2) -> +3.3V
- R48 pad 2: /FT_TDO -> /FTDI/FT_RESET
- R49 pad 1: Net-(U6-ADBUS3) -> /FPGA/REF_CLK
- R49 pad 2: /FT_TMS -> Net-(U6-OSCO)
- R50 pad 1: Net-(U6-BDBUS0) -> Net-(U6-REF)
- R50 pad 2: /FTDI/TXD_UART -> GND
- R51 pad 2: /FTDI/RXD_UART -> +3.3V
- R52 pad 1: Net-(U6-BDBUS0) -> Net-(U6-ADBUS0)
- R52 pad 2: +3.3V -> /FT_TCK
- R53 pad 1: Net-(U6-BDBUS0) -> Net-(U6-ADBUS1)
- R53 pad 2: /FTDI/SCL0 -> /FT_TDI
- R54 pad 1: Net-(U6-BDBUS1) -> Net-(U6-ADBUS2)
- R54 pad 2: /FTDI/SDA0 -> /FT_TDO
- R55 pad 1: Net-(U6-BDBUS2) -> Net-(U6-ADBUS3)
- R55 pad 2: /FTDI/SDA0 -> /FT_TMS
- R56 pad 1: GND -> Net-(U6-BDBUS0)
- R56 pad 2: /FT_TCK -> /FTDI/TXD_UART
- R57 pad 1: +3.3V -> Net-(U6-BDBUS1)
- R57 pad 2: /FT_TDI -> /FTDI/RXD_UART
- R58 pad 1: +3.3V -> Net-(U6-BDBUS0)
- R58 pad 2: /FT_TDO -> +3.3V
- R59 pad 1: +3.3V -> Net-(U6-BDBUS0)
- R59 pad 2: /FT_TMS -> /FTDI/SCL0
- R60 pad 1: /FPGA/sda -> Net-(U6-BDBUS1)
- R60 pad 2: +3.3V -> /FTDI/SDA0
- R61 pad 1: Net-(U3C1C-PR23A/PCLKT2_1) -> Net-(U6-BDBUS2)
- R61 pad 2: /FPGA/SCL0 -> /FTDI/SDA0
- R62 pad 1: Net-(U3C1C-PR23B/PCLKC2_1) -> GND
- R62 pad 2: /FPGA/SDA0 -> /FT_TCK
- R63 pad 1: Net-(U3C1C-PR23C/PCLKT2_0) -> +3.3V
- R63 pad 2: /FPGA/TXD_UART -> /FT_TDI
- R64 pad 1: Net-(U3C1C-PR23D/PCLKC2_0) -> +3.3V
- R64 pad 2: /FPGA/RXD_UART -> /FT_TDO
- R65 pad 1: /FPGA/scl -> +3.3V
- R65 pad 2: +3.3V -> /FT_TMS
- R66 pad 1: SPI_CONFIG_SS -> /FPGA/sda
- R67 pad 1: Net-(U3D1D-PR32A) -> Net-(U8C-PR23A/PCLKT2_1)
- R67 pad 2: /L7 -> /FPGA/SCL0
- R68 pad 1: Net-(U3D1D-PR32B) -> Net-(U8C-PR23B/PCLKC2_1)
- R68 pad 2: /L6 -> /FPGA/SDA0
- R69 pad 1: Net-(U3D1D-PR35A) -> Net-(U8C-PR23C/PCLKT2_0)
- R69 pad 2: /L5 -> /FPGA/TXD_UART
- R70 pad 1: Net-(U3D1D-PR35B/VREF1_3) -> Net-(U8C-PR23D/PCLKC2_0)
- R70 pad 2: /L4 -> /FPGA/RXD_UART
- R71 pad 1: Net-(U3D1D-PR35C) -> /FPGA/scl
- R71 pad 2: /L3 -> +3.3V
- R72 pad 1: Net-(U3D1D-PR35D) -> SPI_CONFIG_SS
- R72 pad 2: /L2 -> +3.3V
- R73 pad 1: Net-(U3D1D-PR38A) -> Net-(U8D-PR32A)
- R73 pad 2: /L1 -> /L7
- R74 pad 1: Net-(U3D1D-PR38B) -> Net-(U8D-PR32B)
- R74 pad 2: /L0 -> /L6
- R75 pad 1: Net-(U3D1D-PR38C) -> Net-(U8D-PR35A)
- R75 pad 2: /K4 -> /L5
- R76 pad 1: Net-(U3D1D-PR38D) -> Net-(U8D-PR35B/VREF1_3)
- R76 pad 2: /K3 -> /L4
- R77 pad 1: Net-(U3D1D-PR41A) -> Net-(U8D-PR35C)
- R77 pad 2: /K2 -> /L3
- R78 pad 1: Net-(U3D1D-PR41B) -> Net-(U8D-PR35D)
- R78 pad 2: /K1 -> /L2
- R79 pad 1: Net-(U3D1D-PR41C) -> Net-(U8D-PR38A)
- R79 pad 2: /ROT_SW -> /L1
- R80 pad 1: Net-(U3D1D-PR41D) -> Net-(U8D-PR38B)
- R80 pad 2: /ROT_B -> /L0
- R81 pad 1: Net-(U3D1D-PR44A) -> Net-(U8D-PR38C)
- R81 pad 2: /ROT_A -> /K4
- R82 pad 1: Net-(U3D1D-PR44B) -> Net-(U8D-PR38D)
- R82 pad 2: /ROT_SW1 -> /K3
- R83 pad 1: Net-(U3D1D-PR44C) -> Net-(U8D-PR41A)
- R83 pad 2: /ROT_B1 -> /K2
- R84 pad 1: Net-(U3D1D-PR44D) -> Net-(U8D-PR41B)
- R84 pad 2: /ROT_A1 -> /K1
- R85 pad 1: Net-(U3G1G-PB13A/SN/CSN) -> Net-(U8D-PR41C)
- R85 pad 2: +3.3V -> /ROT_SW
- R86 pad 1: Net-(U3G1G-PB18A/WRITEN) -> Net-(U8D-PR41D)
- R86 pad 2: +3.3V -> /ROT_B
- R87 pad 1: Net-(U3G1G-PB13B/CS1N) -> Net-(U8D-PR44A)
- R87 pad 2: +3.3V -> /ROT_A
- R88 pad 1: /FPGA PWR/SPI_CONFIG_SCK -> Net-(U8D-PR44B)
- R88 pad 2: +3.3V -> /ROT_SW1
- R89 pad 1: Net-(D10-A) -> Net-(U8D-PR44C)
- R89 pad 2: +3.3V -> /ROT_B1
- R90 pad 1: Net-(U3H1H-CFG_0) -> Net-(U8D-PR44D)
- R90 pad 2: GND -> /ROT_A1
- R91 pad 1: Net-(U3H1H-CFG_1) -> Net-(U8G-PB13A/SN/CSN)
- R92 pad 1: Net-(U3H1H-CFG_2) -> Net-(U8G-PB18A/WRITEN)
- R92 pad 2: GND -> +3.3V
- R93 pad 1: +3.3V -> Net-(U8G-PB13B/CS1N)
- R93 pad 2: Net-(D11-A) -> +3.3V
- R94 pad 1: Net-(Q1-B) -> /FPGA PWR/SPI_CONFIG_SCK
- R94 pad 2: /FPGA PWR/DONE -> +3.3V
- R95 pad 1: /FPGA PWR/INITN -> Net-(D11-A)
- R96 pad 1: /FPGA PWR/DONE -> Net-(U8H-CFG_0)
- R96 pad 2: +3.3V -> GND
- TP10 pad 1: Net-(U3C1C-PR14A) -> Net-(U8C-PR14A)
- TP11 pad 1: Net-(U3C1C-PR14B) -> Net-(U8C-PR14B)
- TP12 pad 1: Net-(U3C1C-PR14C/VREF1_2) -> Net-(U8C-PR14C/VREF1_2)
- TP13 pad 1: Net-(U3C1C-PR14D) -> Net-(U8C-PR14D)
- TP14 pad 1: Net-(U3C1C-PR17A) -> Net-(U8C-PR17A)
- TP15 pad 1: Net-(U3C1C-PR17B) -> Net-(U8C-PR17B)
- TP16 pad 1: Net-(U3C1C-PR20A/GR_PCLK2_1) -> Net-(U8C-PR20A/GR_PCLK2_1)
- TP17 pad 1: Net-(U3C1C-PR20B) -> Net-(U8C-PR20B)
- TP18 pad 1: Net-(U3C1C-PR20C/GR_PCLK2_0) -> Net-(U8C-PR20C/GR_PCLK2_0)
- TP19 pad 1: Net-(U3A1A-PT27A/PCLKT0_1) -> Net-(U8A-PT27A/PCLKT0_1)
- TP2 pad 1: Net-(U3C1C-PR2A) -> Net-(U8C-PR2A)
- TP20 pad 1: Net-(U3A1A-PT27B/PCLKC0_1) -> Net-(U8A-PT27B/PCLKC0_1)
- TP21 pad 1: Net-(U3A1A-PT29A/PCLKT0_0) -> Net-(U8A-PT29A/PCLKT0_0)
- TP22 pad 1: Net-(U3A1A-PT29B/PCLKC0_0) -> Net-(U8A-PT29B/PCLKC0_0)
- TP23 pad 1: Net-(U3B1B-PT33A/PCLKT1_1) -> Net-(U8B-PT33A/PCLKT1_1)
- TP24 pad 1: Net-(U3B1B-PT33B/PCLKC1_1) -> Net-(U8B-PT33B/PCLKC1_1)
- TP25 pad 1: Net-(U3B1B-PT35B/PCLKC1_0) -> Net-(U8B-PT35B/PCLKC1_0)
- TP26 pad 1: Net-(U3B1B-PT67A) -> Net-(U8B-PT67A)
- TP27 pad 1: Net-(U3B1B-PT67B) -> Net-(U8B-PT67B)
- TP28 pad 1: Net-(U3D1D-PR26A/PCLKT3_1) -> Net-(U8D-PR26A/PCLKT3_1)
- TP29 pad 1: Net-(U3D1D-PR26B/PCLKC3_1) -> Net-(U8D-PR26B/PCLKC3_1)
- TP3 pad 1: Net-(U3C1C-PR2B/S0_IN) -> Net-(U8C-PR2B/S0_IN)
- TP30 pad 1: Net-(U3D1D-PR26C/PCLKT3_0) -> Net-(U8D-PR26C/PCLKT3_0)
- TP31 pad 1: Net-(U3D1D-PR26D/PCLKC3_0) -> Net-(U8D-PR26D/PCLKC3_0)
- TP32 pad 1: Net-(U3D1D-PR29A/GR_PCLK3_0) -> Net-(U8D-PR29A/GR_PCLK3_0)
- TP33 pad 1: Net-(U3D1D-PR29B) -> Net-(U8D-PR29B)
- TP34 pad 1: Net-(U3D1D-PR29C/GR_PCLK3_1) -> Net-(U8D-PR29C/GR_PCLK3_1)
- TP35 pad 1: Net-(U3D1D-PR29D) -> Net-(U8D-PR29D)
- TP36 pad 1: Net-(U3G1G-PB4A/D7/IO7) -> Net-(U8G-PB4A/D7/IO7)
- TP37 pad 1: Net-(U3G1G-PB4B/D6/IO6) -> Net-(U8G-PB4B/D6/IO6)
- TP38 pad 1: Net-(U3G1G-PB6A/D5/MISO2/IO5) -> Net-(U8G-PB6A/D5/MISO2/IO5)
- TP39 pad 1: Net-(U3G1G-PB6B/D4/MOSI2/IO4) -> Net-(U8G-PB6B/D4/MOSI2/IO4)
- TP4 pad 1: Net-(U3C1C-PR5A) -> Net-(U8C-PR5A)
- TP40 pad 1: Net-(U3F1F-PL2A) -> Net-(U8F-PL2A)
- TP41 pad 1: Net-(U3F1F-PL2B) -> Net-(U8F-PL2B)
- TP42 pad 1: Net-(U3F1F-PL5A) -> Net-(U8F-PL5A)
- TP43 pad 1: Net-(U3F1F-PL8A) -> Net-(U8F-PL8A)
- TP44 pad 1: Net-(U3F1F-PL8B) -> Net-(U8F-PL8B)
- TP45 pad 1: Net-(U3F1F-PL14A) -> Net-(U8F-PL14A)
- TP46 pad 1: Net-(U3F1F-PL14B) -> Net-(U8F-PL14B)
- TP47 pad 1: Net-(U3F1F-PL14C/VREF1_7) -> Net-(U8F-PL14C/VREF1_7)
- TP48 pad 1: Net-(U3F1F-PL14D) -> Net-(U8F-PL14D)
- TP49 pad 1: Net-(U3F1F-PL17A) -> Net-(U8F-PL17A)
- TP5 pad 1: Net-(U3C1C-PR5B) -> Net-(U8C-PR5B)
- TP50 pad 1: Net-(U3F1F-PL17B) -> Net-(U8F-PL17B)
- TP51 pad 1: Net-(U3F1F-PL20A/GR_PCLK7_1) -> Net-(U8F-PL20A/GR_PCLK7_1)
- TP52 pad 1: Net-(U3F1F-PL20B) -> Net-(U8F-PL20B)
- TP53 pad 1: Net-(U3F1F-PL20C/GR_PCLK7_0) -> Net-(U8F-PL20C/GR_PCLK7_0)
- TP54 pad 1: Net-(U3F1F-PL23A/PCLKT7_1) -> Net-(U8F-PL23A/PCLKT7_1)
- TP55 pad 1: Net-(U3F1F-PL23B/PCLKC7_1) -> Net-(U8F-PL23B/PCLKC7_1)
- TP56 pad 1: Net-(U3F1F-PL23C/PCLKT7_0) -> Net-(U8F-PL23C/PCLKT7_0)
- TP57 pad 1: Net-(U3F1F-PL23D/PCLKC7_0) -> Net-(U8F-PL23D/PCLKC7_0)
- TP58 pad 1: Net-(U3E1E-PL26A/PCLKT6_1) -> Net-(U8E-PL26A/PCLKT6_1)
- TP59 pad 1: Net-(U3E1E-PL26B/PCLKC6_1) -> Net-(U8E-PL26B/PCLKC6_1)
- TP6 pad 1: Net-(U3C1C-PR8A) -> Net-(U8C-PR8A)
- TP60 pad 1: Net-(U3E1E-PL26C/PCLKT6_0) -> Net-(U8E-PL26C/PCLKT6_0)
- TP61 pad 1: Net-(U3E1E-PL26D/PCLKC6_0) -> Net-(U8E-PL26D/PCLKC6_0)
- TP62 pad 1: Net-(U3E1E-PL29A/GR_PCLK6_0) -> Net-(U8E-PL29A/GR_PCLK6_0)
- TP63 pad 1: Net-(U3E1E-PL29B) -> Net-(U8E-PL29B)
- TP64 pad 1: Net-(U3E1E-PL29C/GR_PCLK6_1) -> Net-(U8E-PL29C/GR_PCLK6_1)
- TP65 pad 1: Net-(U3E1E-PL29D) -> Net-(U8E-PL29D)
- TP66 pad 1: Net-(U3E1E-PL32A) -> Net-(U8E-PL32A)
- TP67 pad 1: Net-(U3E1E-PL32B) -> Net-(U8E-PL32B)
- TP68 pad 1: Net-(U3E1E-PL35A) -> Net-(U8E-PL35A)
- TP69 pad 1: Net-(U3E1E-PL35B/VREF1_6) -> Net-(U8E-PL35B/VREF1_6)
- TP7 pad 1: Net-(U3C1C-PR8B) -> Net-(U8C-PR8B)
- TP70 pad 1: Net-(U3E1E-PL35C) -> Net-(U8E-PL35C)
- TP71 pad 1: Net-(U3E1E-PL35D) -> Net-(U8E-PL35D)
- TP72 pad 1: Net-(U3E1E-PL38C) -> Net-(U8E-PL38C)
- TP73 pad 1: Net-(U3E1E-PL38D) -> Net-(U8E-PL38D)
- TP74 pad 1: Net-(U3E1E-PL41A) -> Net-(U8E-PL41A)
- TP75 pad 1: Net-(U3E1E-PL41B) -> Net-(U8E-PL41B)
- TP76 pad 1: Net-(U3E1E-PL41C) -> Net-(U8E-PL41C)
- TP77 pad 1: Net-(U3E1E-PL41D) -> Net-(U8E-PL41D)
- TP78 pad 1: Net-(U3E1E-PL44A) -> Net-(U8E-PL44A)
- TP79 pad 1: Net-(U3E1E-PL44B) -> Net-(U8E-PL44B)
- TP8 pad 1: Net-(U3C1C-PR11A) -> Net-(U8C-PR11A)
- TP80 pad 1: Net-(U3E1E-PL44C) -> Net-(U8E-PL44C)
- TP81 pad 1: Net-(U3E1E-PL44D) -> Net-(U8E-PL44D)
- TP82 pad 1: Net-(U3E1E-PL47C/LLC_GPLL0T_IN) -> Net-(U8E-PL47C/LLC_GPLL0T_IN)
- TP83 pad 1: Net-(U3E1E-PL47D/LLC_GPLL0C_IN) -> Net-(U8E-PL47D/LLC_GPLL0C_IN)
- TP9 pad 1: Net-(U3C1C-PR11B) -> Net-(U8C-PR11B)
- U1 pad 1: Net-(U1-TS) -> Net-(U1-FB)
- U1 pad 2: VBATT -> GND
- U1 pad 3: VBATT -> VSYS
- U1 pad 4: GND -> Net-(U1-SW)
- U1 pad 5: VSYS -> EN
- U1 pad 6: GND -> unconnected-(U1-NC-Pad6)
- U3 pad 1: Net-(U3-FB) -> +2.5V
- U3 pad 3: VSYS -> EN
- U3 pad 4: Net-(U3-SW) -> +3.3V
- U3 pad 5: EN -> (no net)
- U4 pad 1: +2.5V -> Net-(U4-TS)
- U4 pad 2: GND -> VBATT
- U4 pad 3: EN -> VBATT
- U4 pad 4: +3.3V -> GND
- U4 pad 5: (no net) -> VSYS

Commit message: Complete pn asignent. Start routing
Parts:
- C26, C27, C29, C31, R48, R50: moved to B.Cu
- moved R64 121.7 mm to (66.8, 162.4), turned to 90 degrees
- moved R65 119.0 mm to (68.6, 162.4), turned to 90 degrees
- moved R62 111.7 mm to (63.4, 162.4), turned to 90 degrees
- moved R63 109.0 mm to (65.1, 162.4), turned to 90 degrees
- moved R60 103.8 mm to (86.0, 150.7)
- moved R61 100.0 mm to (82.0, 149.6)
- moved TP24 95.8 mm to (154.8, 43.0)
- moved TP25 95.8 mm to (154.8, 46.6)
- moved TP26 95.8 mm to (154.8, 50.1)
- moved TP27 95.8 mm to (154.8, 53.7)
- moved TP28 95.8 mm to (154.8, 57.2)
- moved TP29 95.8 mm to (154.8, 60.8)
- moved TP30 95.8 mm to (154.8, 64.3)
- moved TP31 95.8 mm to (154.8, 67.9)
- moved TP32 95.8 mm to (154.8, 71.5)
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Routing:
- net +3.3V: track 0.00 -> 13.4 mm, vias 0 -> 5
- net Net-(U6-BDBUS1): track 0.00 -> 10.8 mm
- net /FTDI/EE_DAT: track 0.00 -> 9.94 mm, vias 0 -> 2
- net Net-(U6-OSCI): track 0.00 -> 9.59 mm
- net /FTDI/EE_CS: track 0.00 -> 9.14 mm
- net Net-(U6-OSCO): track 0.00 -> 8.84 mm
- net Net-(U6-ADBUS0): track 0.00 -> 7.14 mm
- net GND: track 0.00 -> 6.95 mm, vias 0 -> 8
- net Net-(U6-BDBUS0): track 0.00 -> 6.94 mm
- net Net-(U6-ADBUS1): track 0.00 -> 5.69 mm
- net /FTDI/SDA0: track 0.00 -> 5.07 mm
- net Net-(U6-ADBUS2): track 0.00 -> 4.36 mm
- net Net-(U5-DO): track 0.00 -> 4.25 mm
- net /FTDI/EE_CLK: track 0.00 -> 3.87 mm
- net Net-(U6-BDBUS2): track 0.00 -> 3.41 mm
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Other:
- copper layers 2 -> 4

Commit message: Continue routing
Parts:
- added U10: XC6206PxxxMR, Package_TO_SOT_SMD:SOT-23-3, F.Cu at (212.1, 50.8)
- moved C39 171.3 mm to (227.4, 132.8)
- moved R72 160.1 mm to (223.8, 132.8)
- moved U9 155.1 mm to (225.5, 136.7)
- moved R97 111.3 mm to (201.8, 132.4), turned to 90 degrees
- moved R98 110.5 mm to (203.8, 132.2), turned to -90 degrees
- moved C38 105.0 mm to (167.4, 101.0)
- moved U3 103.6 mm to (211.4, 54.2)
- moved C13 102.2 mm to (205.3, 53.8)
- moved R66 100.8 mm to (167.4, 104.6)
- moved C14 99.9 mm to (219.8, 37.2)
- moved C16 99.9 mm to (207.5, 36.0)
- moved C9 99.9 mm to (207.5, 31.0)
- moved R27 99.9 mm to (207.5, 43.5)
- moved C18 99.9 mm to (202.7, 38.1)
- moved L1 99.9 mm to (216.9, 46.2)
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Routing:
- net GND: track 6.95 -> 98.4 mm, vias 8 -> 70
- net Net-(U8E-PL41D): track 0.00 -> 13.2 mm, vias 0 -> 1
- net Net-(U8E-PL35C): track 0.00 -> 9.72 mm, vias 0 -> 1
- net Net-(U8E-PL35B/VREF1_6): track 0.00 -> 9.62 mm, vias 0 -> 1
- net Net-(U8E-PL41C): track 0.00 -> 9.57 mm, vias 0 -> 1
- net Net-(U8E-PL44A): track 0.00 -> 9.25 mm
- net Net-(U8E-PL35D): track 0.00 -> 9.18 mm, vias 0 -> 1
- net Net-(U8E-PL38C): track 0.00 -> 9.15 mm
- net Net-(U8E-PL38D): track 0.00 -> 9.10 mm
- net Net-(U8E-PL29D): track 0.00 -> 9.01 mm, vias 0 -> 1
- net Net-(U8E-PL41A): track 0.00 -> 8.88 mm
- net Net-(U8E-PL32B): track 0.00 -> 8.58 mm
- net Net-(U8E-PL32A): track 0.00 -> 7.90 mm
- net Net-(U8F-PL23D/PCLKC7_0): track 0.00 -> 6.31 mm
- net Net-(U8F-PL23B/PCLKC7_1): track 0.00 -> 5.52 mm
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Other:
- board outline added: 245.2 x 139.3 mm

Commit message: Continue routing
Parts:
- R91, R92, R93, R94: moved to B.Cu
- moved C1 153.3 mm to (185.0, 190.4)
- moved C2 153.3 mm to (182.7, 190.7)
- moved C22 153.3 mm to (200.7, 175.9)
- moved C23 153.3 mm to (194.2, 176.9)
- moved C24 153.3 mm to (188.2, 176.9)
- moved C25 153.3 mm to (206.2, 177.9)
- moved C26 153.3 mm to (203.2, 182.7)
- moved C27 153.3 mm to (201.9, 186.4)
- moved C28 153.3 mm to (197.7, 194.2)
- moved C31 153.3 mm to (199.7, 182.7)
- moved C32 153.3 mm to (202.7, 193.6)
- moved C33 153.3 mm to (204.8, 194.3)
- moved C34 153.3 mm to (188.4, 180.9)
- moved C35 153.3 mm to (188.4, 187.4)
- moved C36 153.3 mm to (190.4, 180.9)
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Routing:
- net Net-(U8E-PL26D/PCLKC6_0): track 1.16 -> 24.2 mm
- net Net-(U8E-PL29A/GR_PCLK6_0): track 1.74 -> 21.7 mm
- net Net-(U8E-PL41B): track 0.80 -> 19.7 mm
- net Net-(U8E-PL29B): track 2.65 -> 21.2 mm, vias 1 -> 0
- net Net-(U8G-PB6B/D4/MOSI2/IO4): track 1.10 -> 17.3 mm
- net Net-(U8E-PL35A): track 2.60 -> 18.8 mm
- net Net-(U8E-PL44B): track 1.10 -> 15.7 mm
- net Net-(U8E-PL38D): track 9.10 -> 22.2 mm
- net Net-(U8E-PL41D): track 13.2 -> 0.28 mm
- net Net-(U8E-PL47D/LLC_GPLL0C_IN): track 1.70 -> 13.9 mm
- net Net-(U8E-PL44D): track 2.17 -> 13.9 mm, vias 1 -> 0
- net Net-(U8E-PL32A): track 7.90 -> 19.4 mm
- net Net-(U8E-PL29D): track 9.01 -> 19.8 mm
- net Net-(U8E-PL32B): track 8.58 -> 18.4 mm
- net Net-(U8E-PL41A): track 8.88 -> 16.6 mm
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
